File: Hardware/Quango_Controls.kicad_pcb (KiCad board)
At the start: 2 copper layers, 80.9 x 128.5 mm, 36 parts, among them J1 Conn_01x12_Male, J2 Conn_01x12_Male, J3 Conn_01x12_Male, J4 Conn_01x12_Male, J5 CV_A, J6 CV_B, J7 Out, J8 USB_C_Receptacle, J9 Midi_In, SW1 SW_Push, SW2 SW_Push

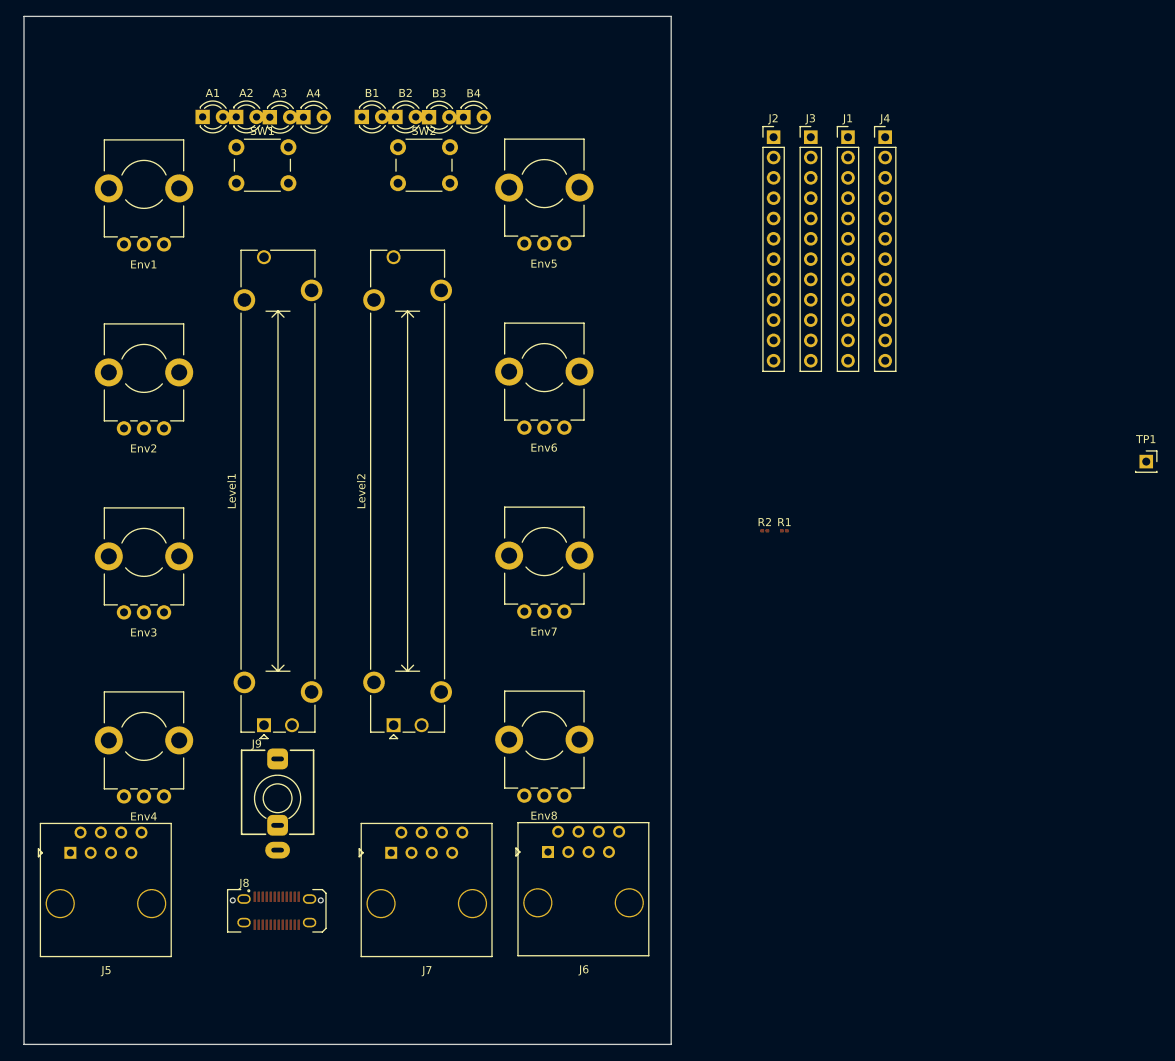
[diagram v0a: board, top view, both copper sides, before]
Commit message: Reduced module size to 14HP; updated to Amphenol USB C
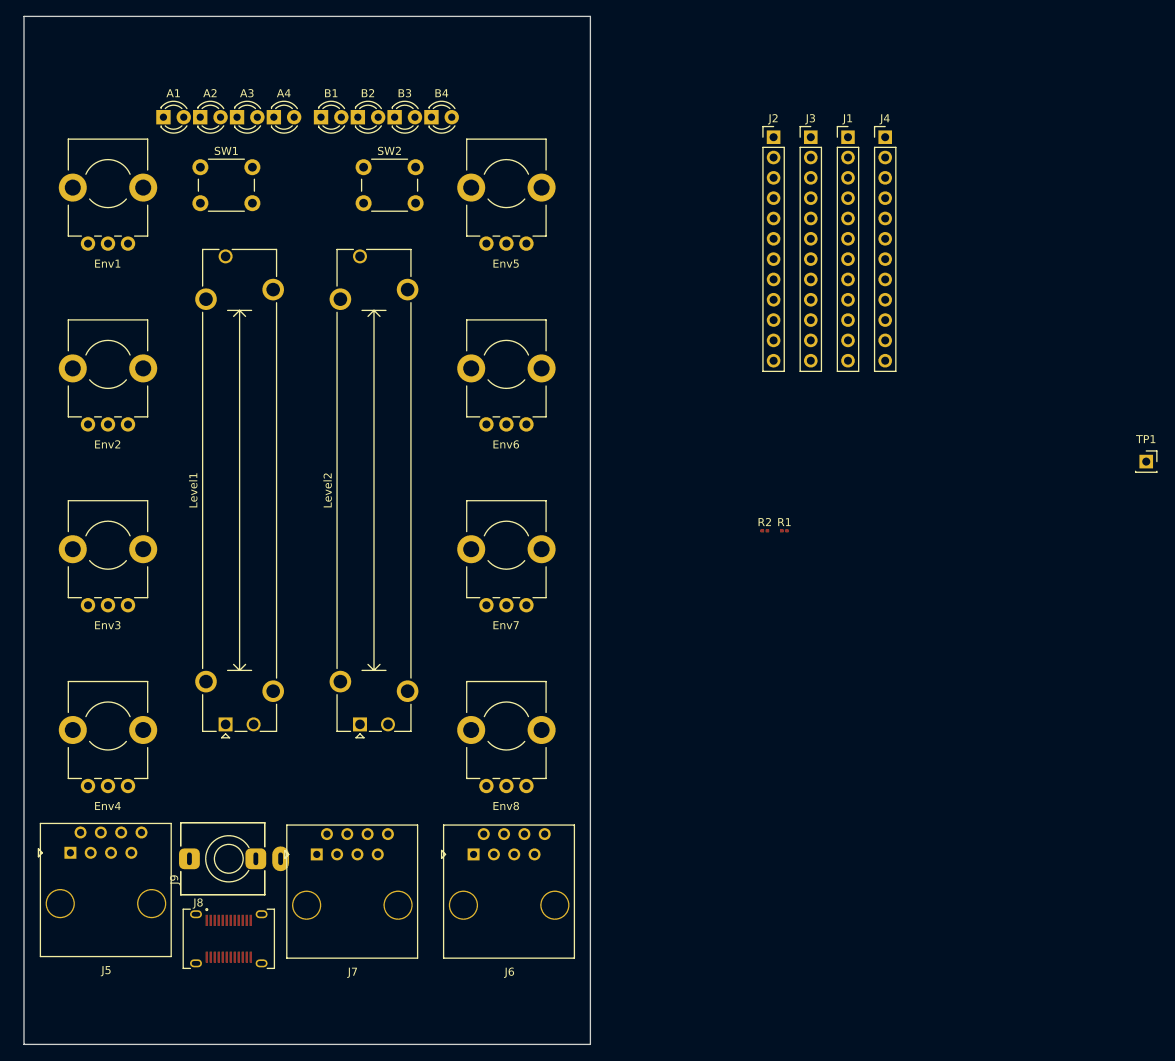
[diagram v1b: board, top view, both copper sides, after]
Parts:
- J8: footprint Connector_USB:USB_C_Receptacle_JAE_DX07S024WJ3R400 -> Custom_Footprints:USB_C_Receptacle_Amphenol_12401951E412A
- moved J9 9.72 mm to (75.6, 135.3), turned to 90 degrees
- moved J6 9.30 mm to (110.6, 139.4)
- moved J7 9.30 mm to (91.0, 139.4)
- moved J8 6.95 mm to (75.6, 145.3)
- moved SW1 5.15 mm to (75.3, 51.1)
- moved B1 5.10 mm to (88.4, 42.6)
- moved SW2 4.97 mm to (95.7, 51.1)
- moved A1 4.90 mm to (68.7, 42.6)
- moved Env8 4.89 mm to (110.3, 118.7)
- moved Env7 4.81 mm to (110.3, 96.1)
- moved Level1 4.80 mm to (75.2, 118.5)
- moved Env6 4.76 mm to (110.3, 73.5)
- moved Env5 4.74 mm to (110.3, 50.9)
- moved B2 4.70 mm to (93.0, 42.6)
- moved Env4 4.68 mm to (60.5, 118.7)
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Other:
- board size 80.9 x 128.5 mm -> 70.8 x 128.5 mm

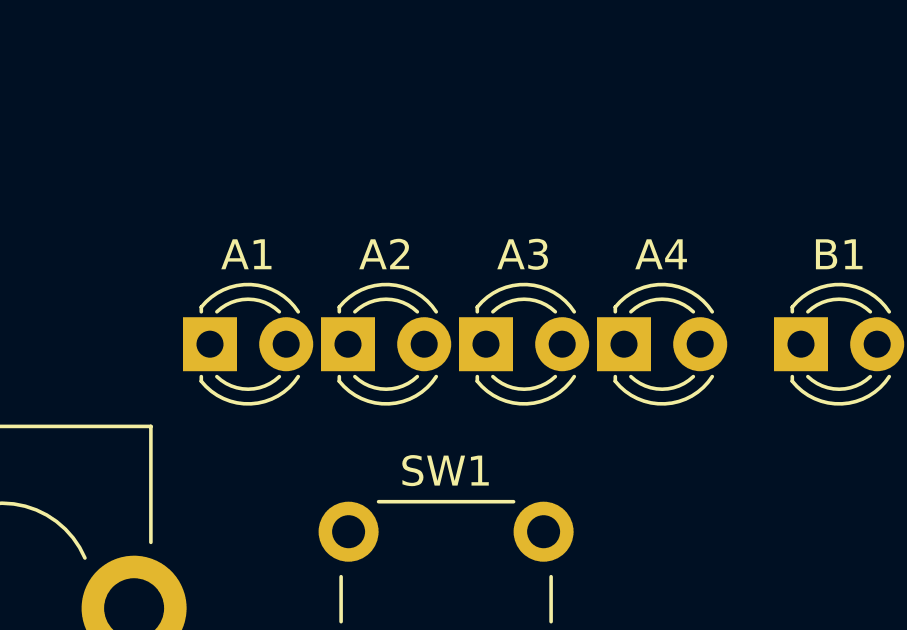
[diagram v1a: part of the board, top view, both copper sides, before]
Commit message: Added individual audio channel breakout
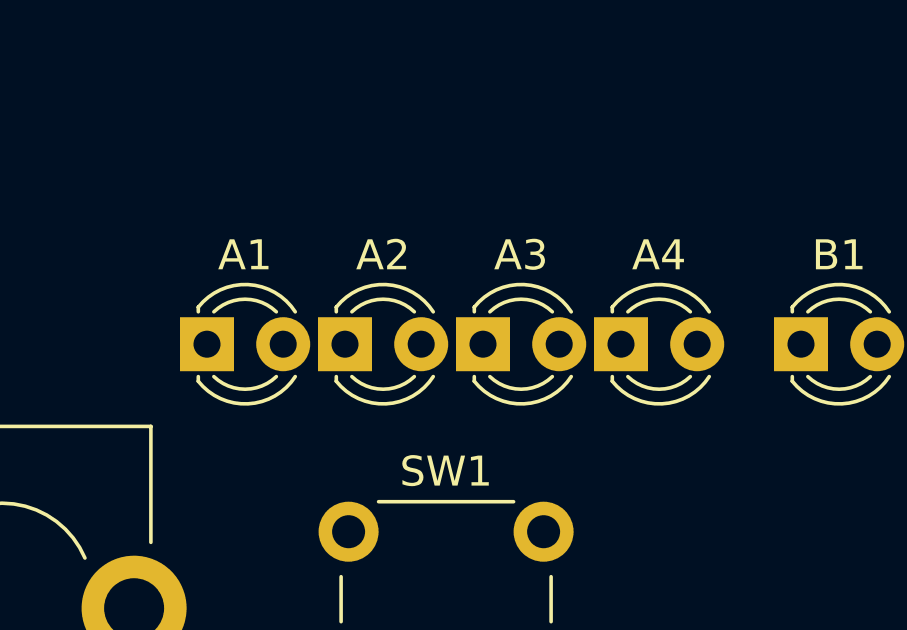
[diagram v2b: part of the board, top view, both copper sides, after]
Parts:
- moved A1 0.10 mm to (68.6, 42.6)
- moved A3 0.10 mm to (77.8, 42.6)
- moved A2 0.10 mm to (73.2, 42.6)
- moved A4 0.10 mm to (82.4, 42.6)
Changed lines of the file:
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@@
   (net 63 "unconnected-(J9-PadR)")
   (footprint "Custom_Footprints:LED_D3.0mm" (layer "F.Cu")
-    (at 77.9 42.6)
+    (at 77.8 42.6)
     (descr "LED, diameter 3.0mm, 2 pins")
     (tags "LED diameter 3.0mm 2 pins")
@@
   )
   (footprint "Custom_Footprints:LED_D3.0mm" (layer "F.Cu")
-    (at 82.5 42.6)
+    (at 82.4 42.6)
     (descr "LED, diameter 3.0mm, 2 pins")
     (tags "LED diameter 3.0mm 2 pins")
@@
   )
   (footprint "Custom_Footprints:LED_D3.0mm" (layer "F.Cu")
-    (at 68.7 42.6)
+    (at 68.6 42.6)
     (descr "LED, diameter 3.0mm, 2 pins")
     (tags "LED diameter 3.0mm 2 pins")
@@
   )
   (footprint "Custom_Footprints:LED_D3.0mm" (layer "F.Cu")
-    (at 73.3 42.6)
+    (at 73.2 42.6)
     (descr "LED, diameter 3.0mm, 2 pins")
     (tags "LED diameter 3.0mm 2 pins")
@@
     )
   )
-  (gr_rect (start 50.1 39) (end 130.8 149) (layer "Dwgs.User") (width 0.15) (fill none))
+  (gr_rect (start 50.1 39) (end 120.8 149) (layer "Dwgs.User") (width 0.15) (fill none))
+  (gr_line locked (start 85.4 28.6) (end 85.4 160.2) (layer "Dwgs.User") (width 0.15))
   (gr_rect (start 50 30) (end 120.8 158.5) (layer "Edge.Cuts") (width 0.1) (fill none))
 )

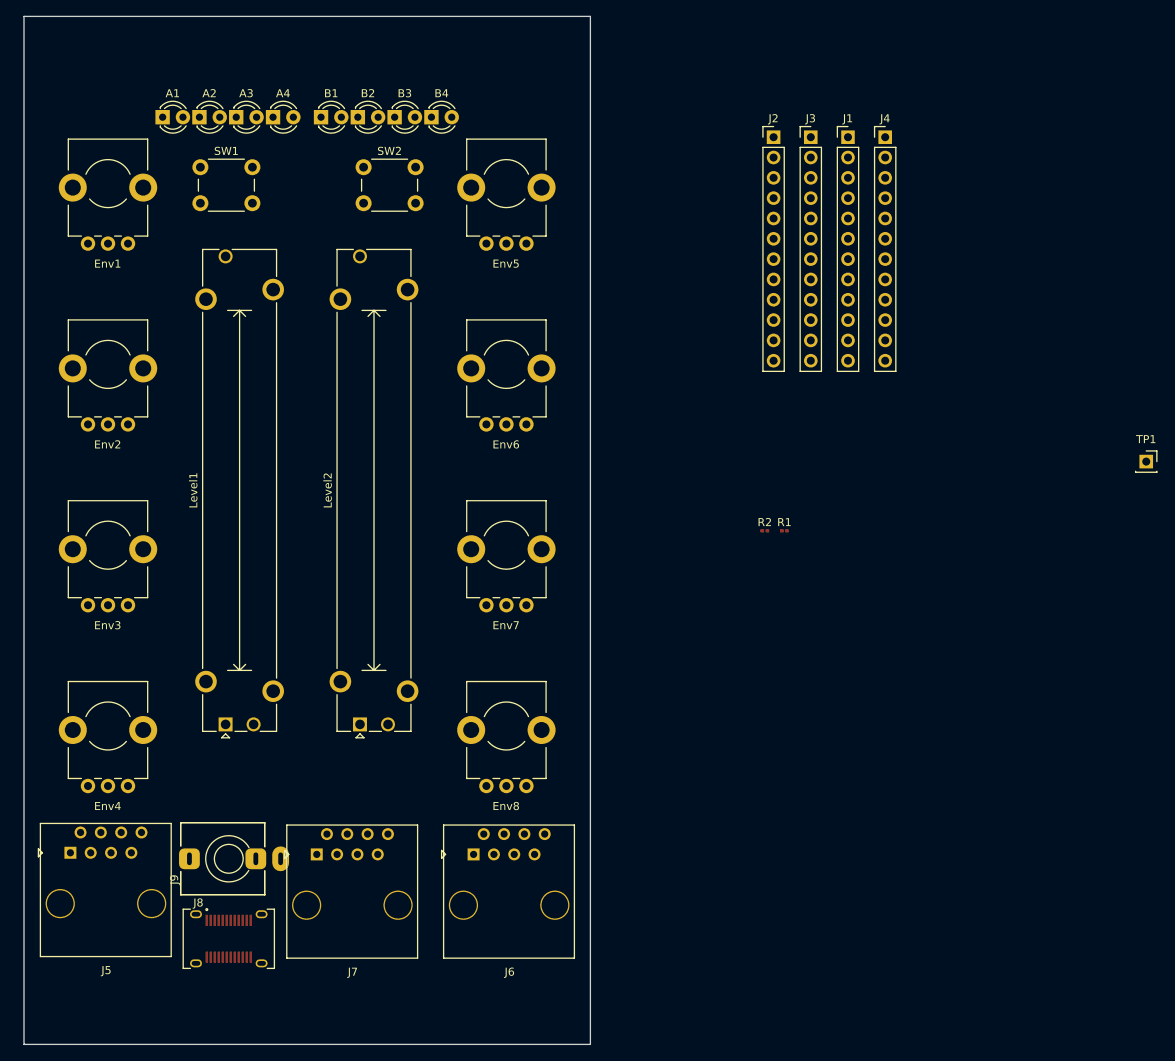
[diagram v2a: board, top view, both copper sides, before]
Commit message: Preparing panel and control board for routing
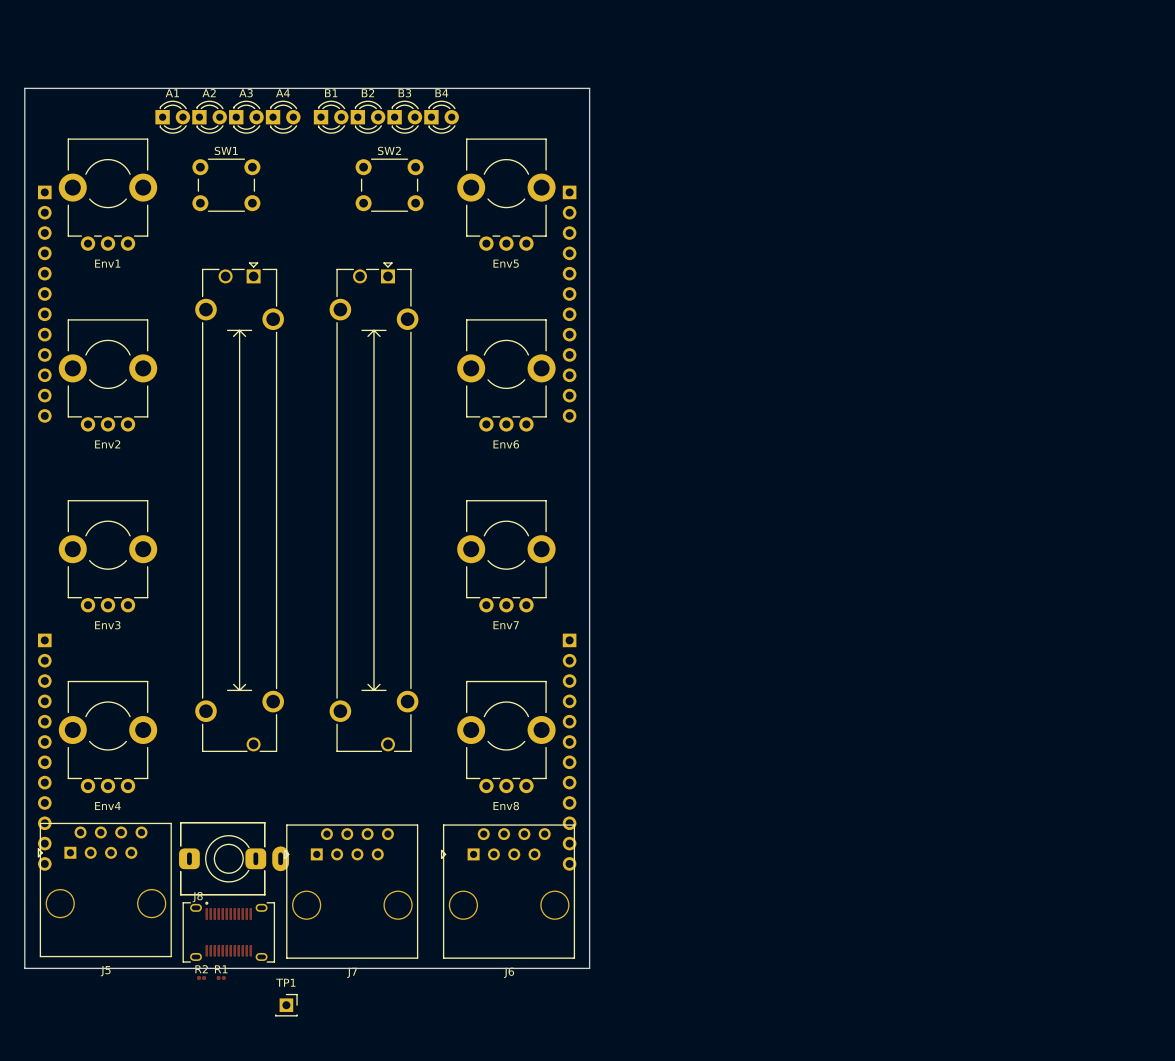
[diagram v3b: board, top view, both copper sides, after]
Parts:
- removed Ref** (x4): Oval_Mounting_Hole, Custom_Footprints:Oval_Mounting_Hole
- J1, J2, J3, J4: moved to B.Cu
- moved TP1 127.2 mm to (82.8, 153.6)
- moved J4 122.4 mm to (52.6, 108.0), turned to 180 degrees
- moved J3 96.0 mm to (52.6, 52.0), turned to 180 degrees
- moved R1 89.9 mm to (74.7, 150.2)
- moved R2 89.9 mm to (72.2, 150.2)
- moved J2 67.9 mm to (118.2, 108.0), turned to 180 degrees
- moved Level1 56.1 mm to (78.7, 62.5), turned to -90 degrees
- moved Level2 56.1 mm to (95.5, 62.5), turned to -90 degrees
- moved J1 35.5 mm to (118.2, 52.0), turned to 180 degrees
- moved J8 0.80 mm to (75.6, 144.5)
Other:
- board size 70.8 x 128.5 mm -> 70.6 x 110 mm

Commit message: First draft routing of control board
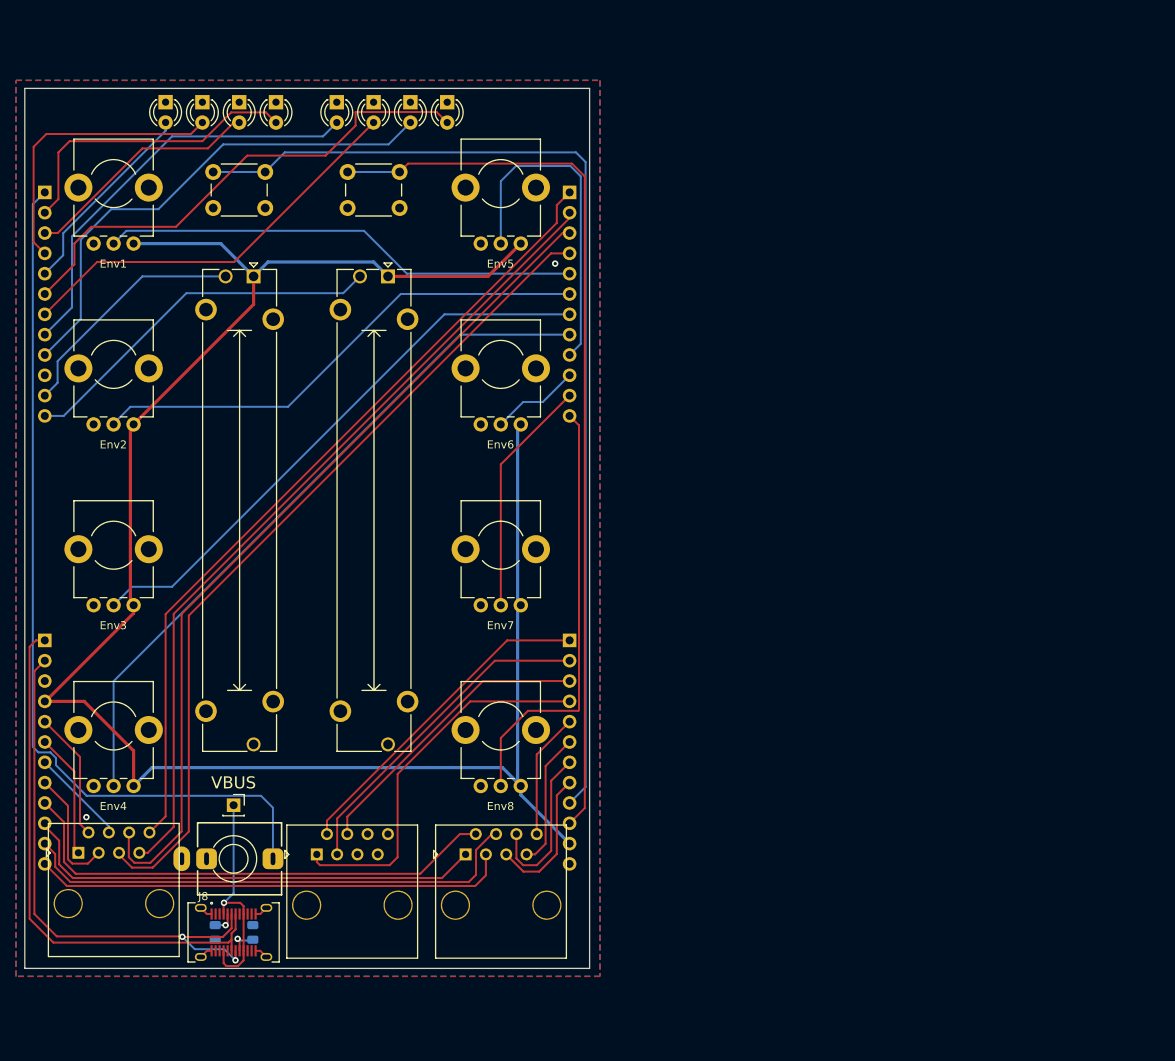
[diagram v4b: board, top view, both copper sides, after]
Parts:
- R1, R2: footprint Resistor_SMD:R_0201_0603Metric -> Resistor_SMD:R_0805_2012Metric; moved to B.Cu
- moved TP1 25.9 mm to (76.2, 128.6)
- moved R2 8.57 mm to (78.6, 144.5), turned to 90 degrees
- moved R1 5.75 mm to (73.9, 144.5), turned to -90 degrees
- moved SW2 2.09 mm to (93.7, 51.7)
- moved SW1 1.71 mm to (76.9, 51.7)
- moved A1 1.09 mm to (67.7, 42.0), turned to -90 degrees
- moved A2 1.08 mm to (72.3, 42.0), turned to -90 degrees
- moved A4 1.08 mm to (81.5, 42.0), turned to -90 degrees
- moved A3 1.08 mm to (76.9, 42.0), turned to -90 degrees
- moved J5 1.00 mm to (61.2, 139.2)
- moved J6 1.00 mm to (109.6, 139.4)
- moved B2 0.92 mm to (93.7, 42.0), turned to -90 degrees
- moved B3 0.92 mm to (98.3, 42.0), turned to -90 degrees
- moved B4 0.92 mm to (102.9, 42.0), turned to -90 degrees
- moved B1 0.92 mm to (89.1, 42.0), turned to -90 degrees
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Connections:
- J2 pad 11: /MIDI_IN -> +3.3VA
- J3 pad 1: /EnvB4_LED_Out -> /MIDI_IN
- J3 pad 2: /EnvB3_LED_Out -> /EnvA4_LED_Out
- J3 pad 3: /EnvB2_LED_Out -> /EnvA3_LED_Out
- J3 pad 4: /EnvB1_LED_Out -> /EnvA2_LED_Out
- J3 pad 5: /EnvA4_LED_Out -> /EnvA1_LED_Out
- J3 pad 6: /EnvA2_LED_Out -> /EnvB4_LED_Out
- J3 pad 7: /EnvA1_LED_Out -> /EnvB2_LED_Out
- J3 pad 8: /EnvA3_LED_Out -> /EnvB1_LED_Out
- J3 pad 9: +3.3VA -> /EnvB3_LED_Out
- J4 pad 1: /USB_DP -> /USB_DM
- J4 pad 2: /USB_DM -> /USB_DP
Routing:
- net +3.3VA: track 0.00 -> 241.6 mm
- net /Calib_Btn1: track 0.00 -> 129.0 mm
- net /Calib_Btn2: track 0.00 -> 112.4 mm
- net /MIDI_IN: track 0.00 -> 110.0 mm
- net /AudioA2_In: track 0.00 -> 107.0 mm
- net /AudioA1_In: track 0.00 -> 104.8 mm
- net /AudioA3_In: track 0.00 -> 102.9 mm
- net /AudioA4_In: track 0.00 -> 101.8 mm
- net /Env1_Release: track 0.00 -> 88.0 mm
- net /Env1_Sustain: track 0.00 -> 72.1 mm
- net /USB_DP: track 0.00 -> 69.4 mm, vias 0 -> 2
- net /USB_DM: track 0.00 -> 67.7 mm
- net /Env1_Decay: track 0.00 -> 63.8 mm
- net /CV_OUT_B4: track 0.00 -> 63.6 mm
- net /EnvB3_LED_Out: track 0.00 -> 63.5 mm
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- added copper zone on B.Cu, net GND
- added copper zone on F.Cu, net GND
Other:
- board text added: "VBUS"
